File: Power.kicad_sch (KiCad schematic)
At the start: 25 parts, among them Q1 Si2371EDS, Q2 DMG9926UDM, U5 LP5907MFX-3.3, U6 MCP73831-2-MC, U7 BQ29700

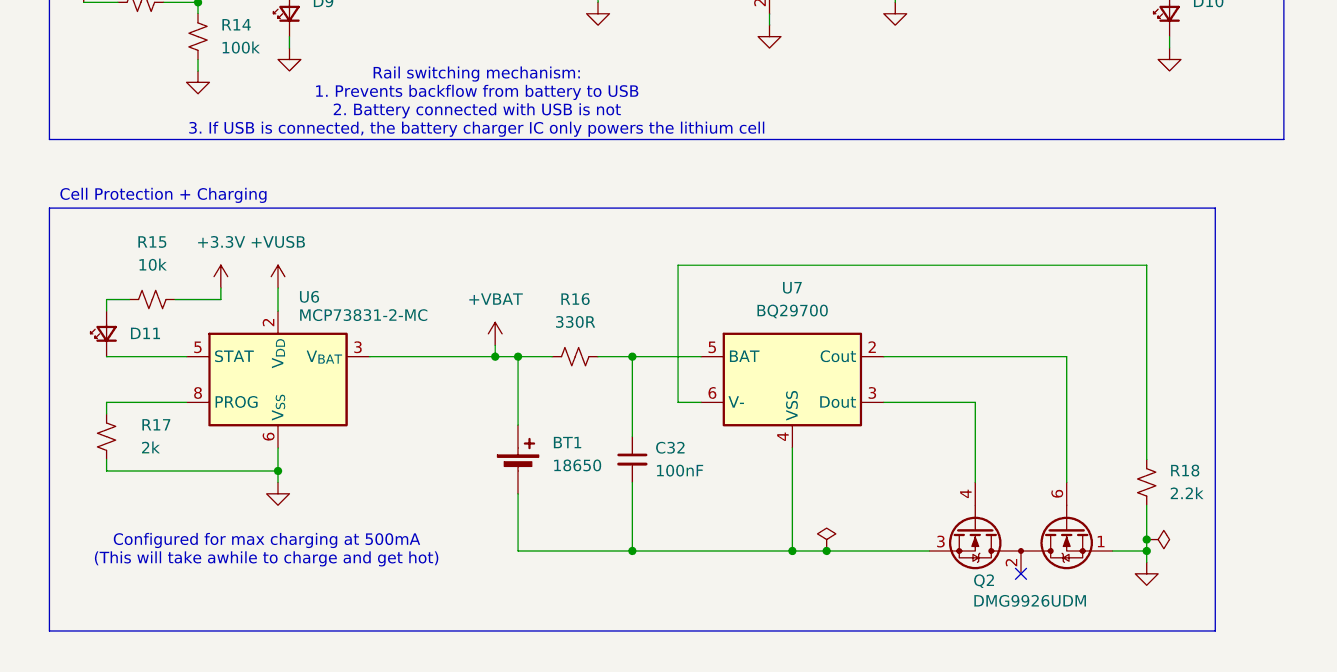
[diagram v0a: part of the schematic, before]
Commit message: Add buzzer, fix some erc
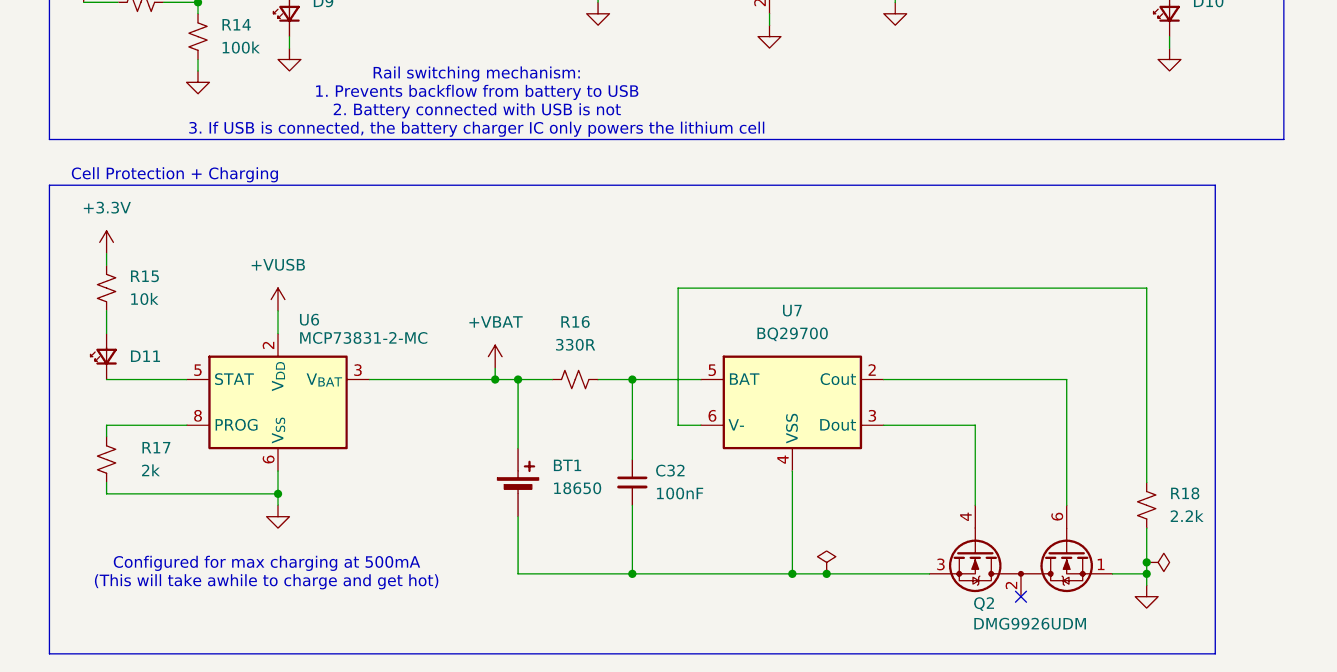
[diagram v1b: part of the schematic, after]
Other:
- moved on the sheet: BT1, C32, D11, Q2, R15, R16, R17, R18, U6, U7

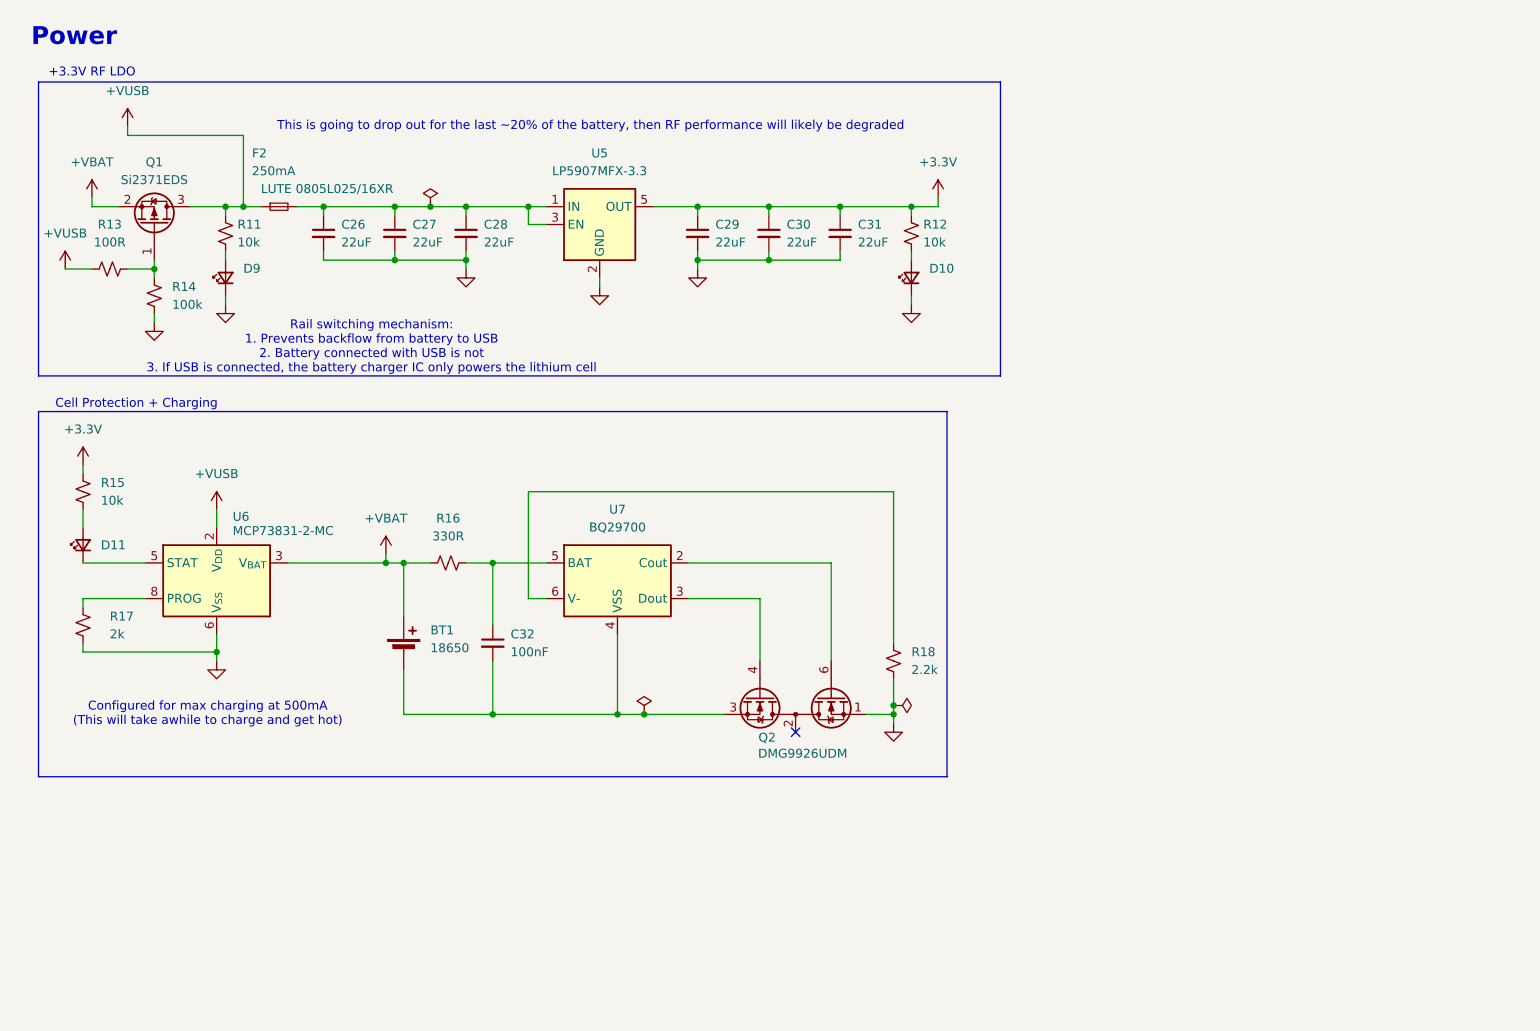
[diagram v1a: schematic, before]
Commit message: Add external 3.3V selector (noise is not real anyway)
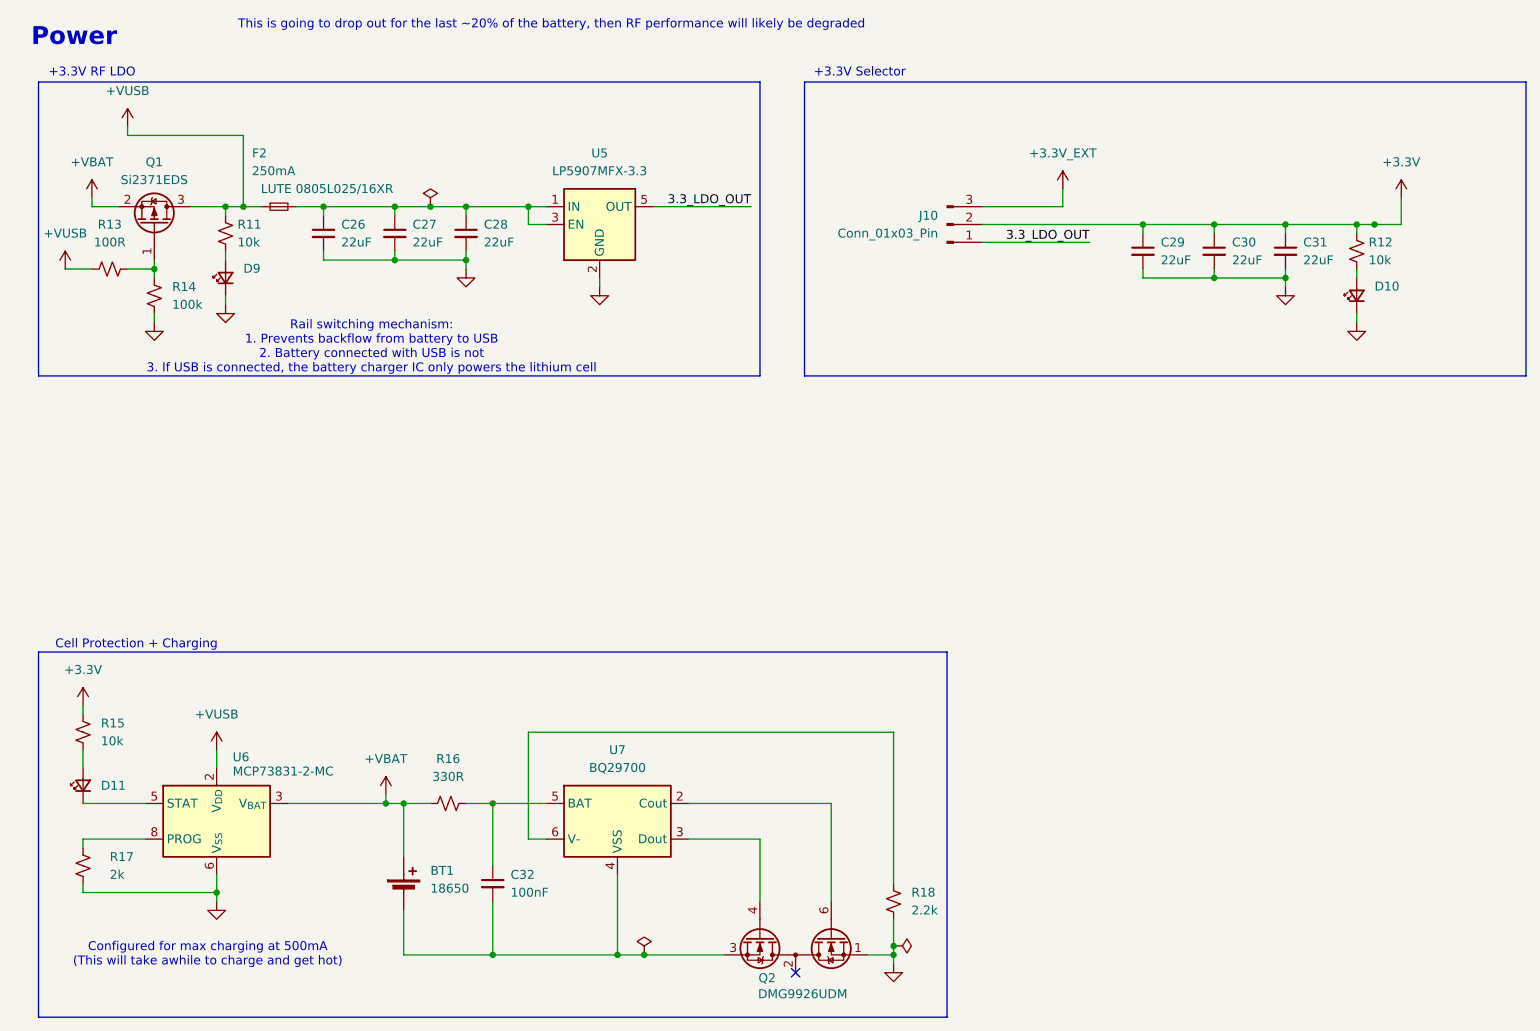
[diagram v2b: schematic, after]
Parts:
- added J10: Conn_01x03_Pin, Connector_PinHeader_2.54mm:PinHeader_1x03_P2.54mm_Vertical, symbol Connector:Conn_01x03_Pin
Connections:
- net +3.3V: now also J10.2 (Pin_2); no longer U5.5 (OUT)
- new net +3.3V_EXT: J10.3 (Pin_3)
- new net 3.3_LDO_OUT: J10.1 (Pin_1), U5.5 (OUT)
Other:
- note added: "+3.3V Selector"
- moved on the sheet: BT1, C32, D11, Q2, R15, R16, R17, R18, U6, U7
